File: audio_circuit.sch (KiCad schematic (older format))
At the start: 19 parts

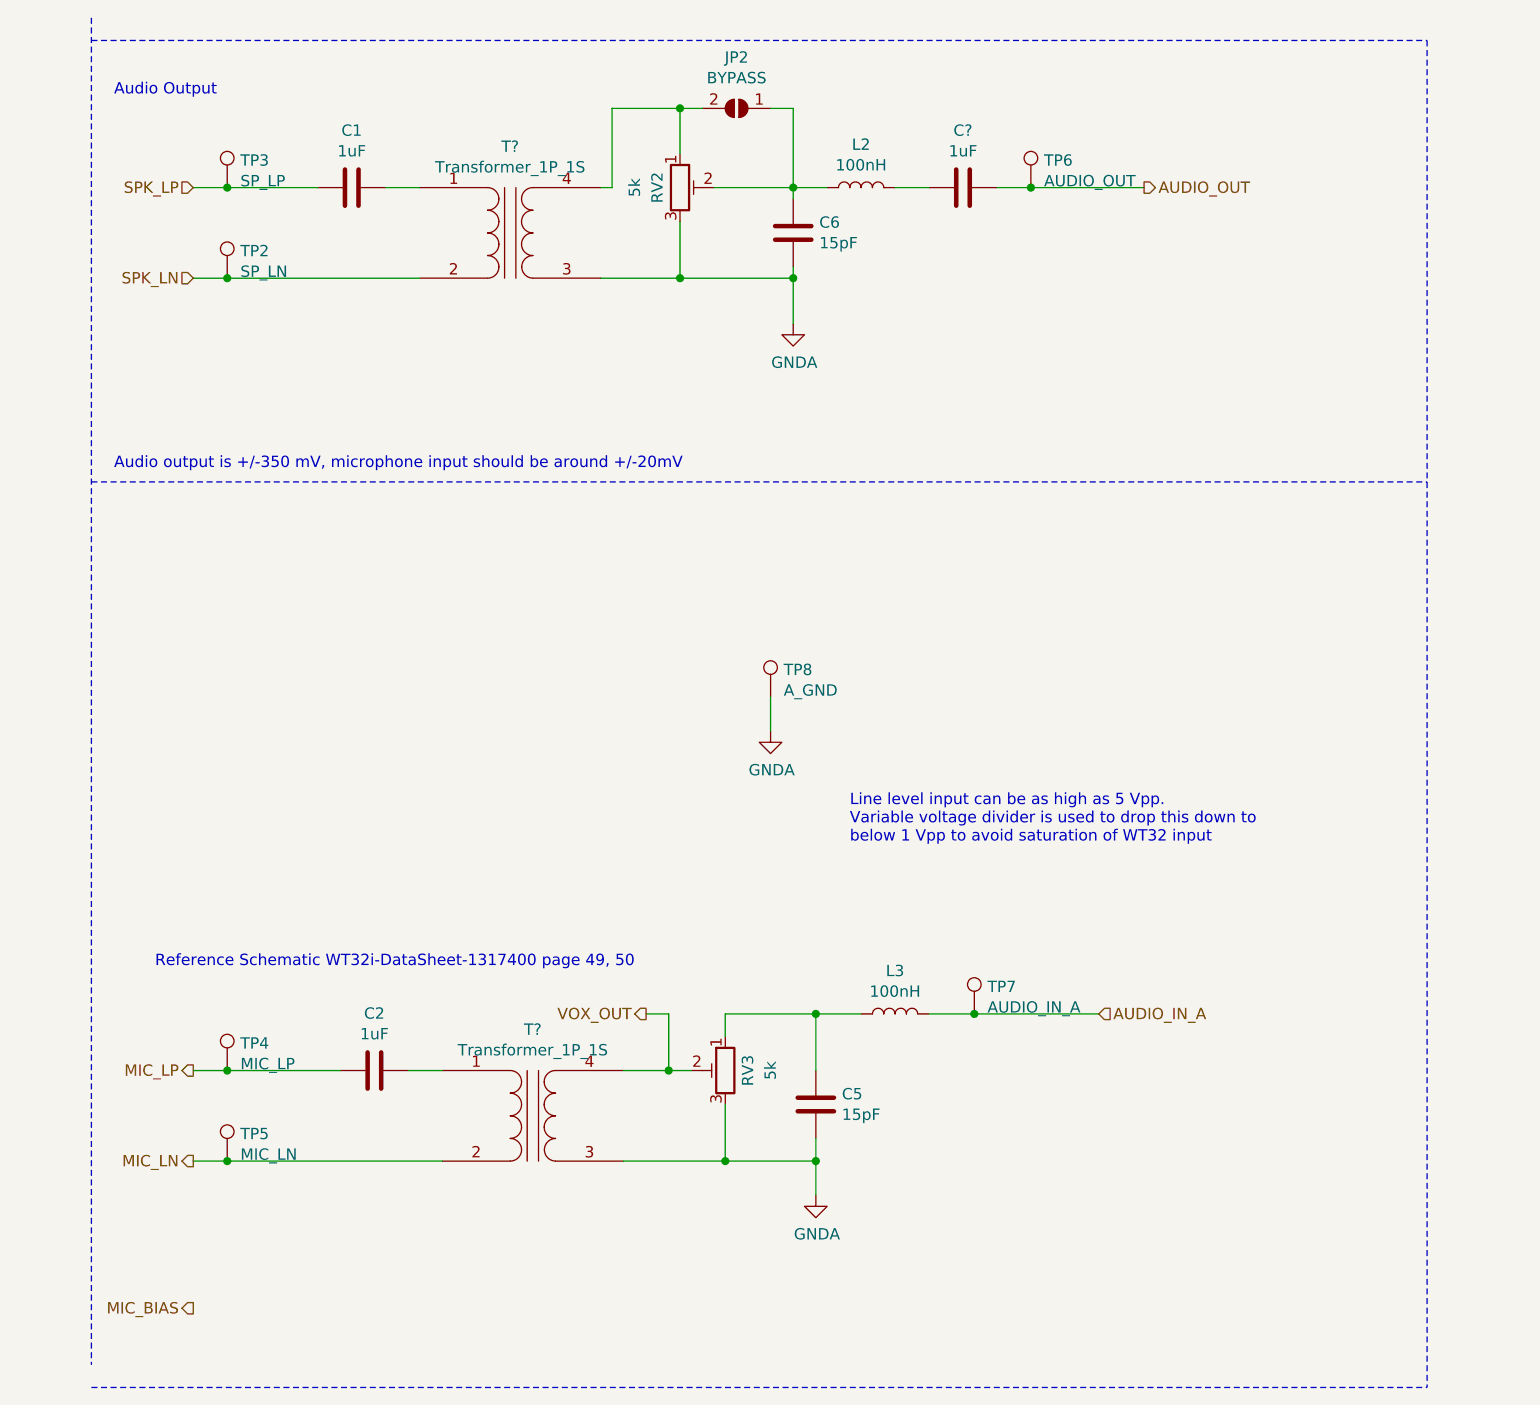
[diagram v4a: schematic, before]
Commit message: Further Audio Rework, separation of AGND and MIC_GND [#21]
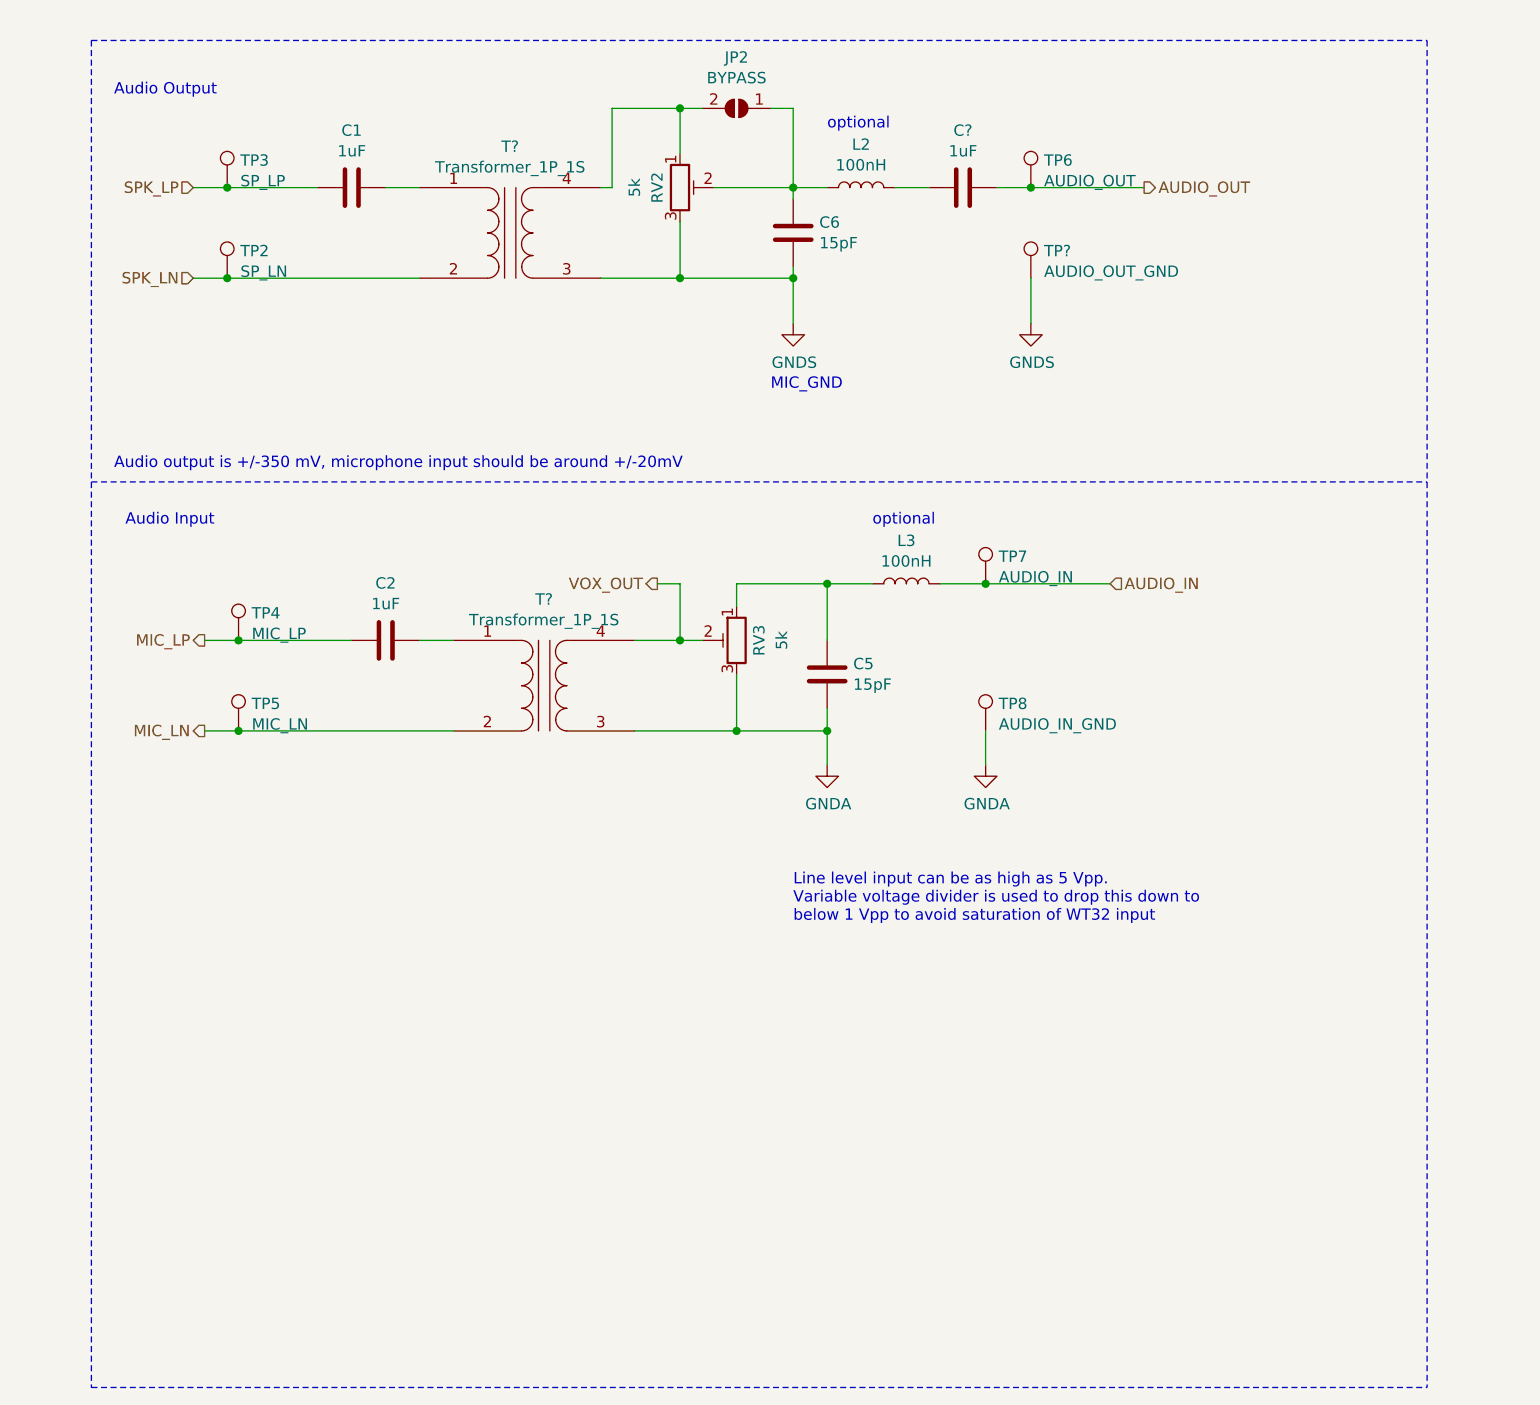
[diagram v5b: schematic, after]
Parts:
- added TP?: AUDIO_OUT_GND, TestPoint:TestPoint_Pad_4.0x4.0mm, symbol Connector:TestPoint
- TP7: value AUDIO_IN_A -> AUDIO_IN
- TP8: value A_GND -> AUDIO_IN_GND
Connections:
- net GNDA: no longer C6.2, RV2.3, T?.3 (SA)
- net AUDIO_IN_A renamed AUDIO_IN
- new net GNDS: C6.2, RV2.3, T?.3 (SA), TP?.1
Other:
- note added: "Audio Input"
- note added: "MIC_GND"
- note added: "optional"
- note removed: "Reference Schematic WT32i-DataSheet-1317400 page 49, 50"
- moved on the sheet: C2, C5, L3, RV3, T?, TP4, TP5, TP7, TP8

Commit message: Continued Schematic for V5.0
* Rearanged RJ45 connector
* Added jumper wire connector
* Renamed GNDs
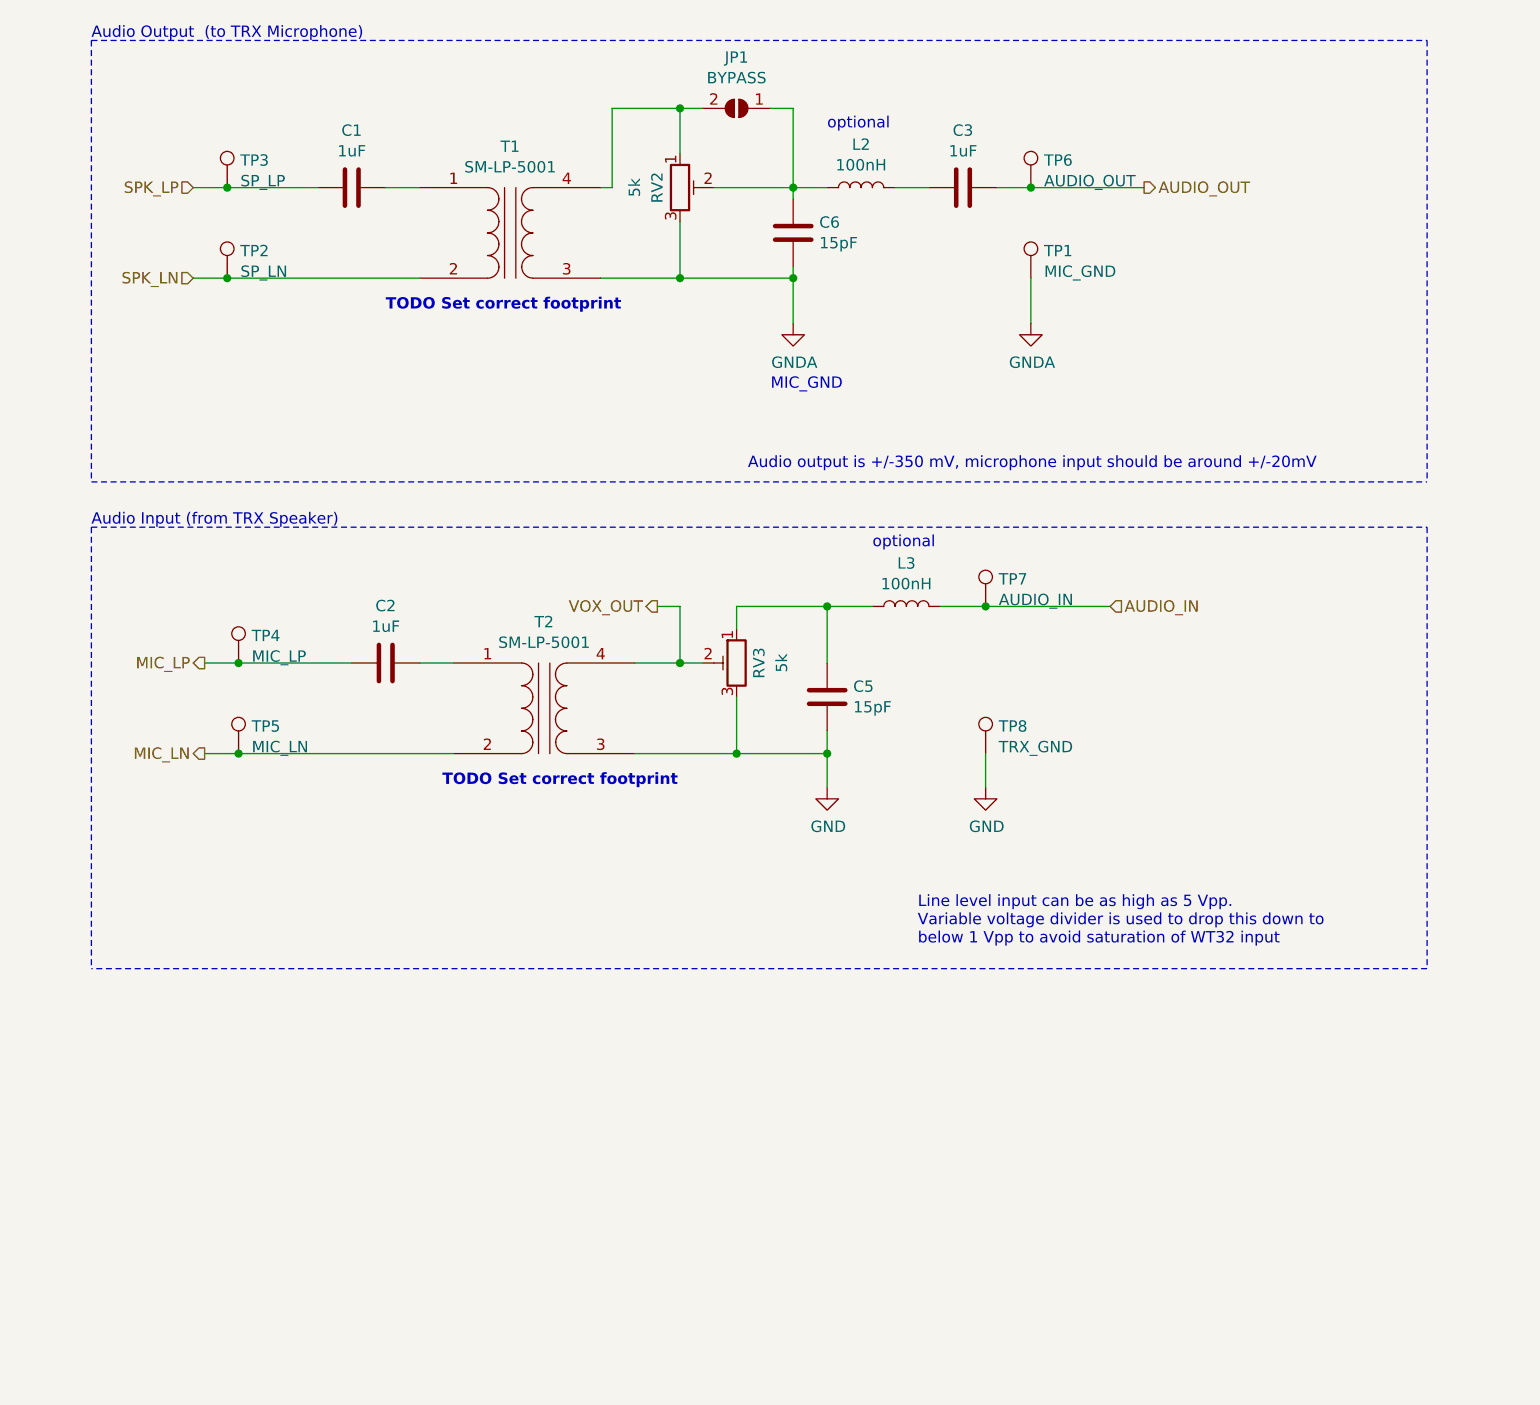
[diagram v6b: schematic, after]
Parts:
- T1, T2: renamed from T?; value Transformer_1P_1S -> SM-LP-5001
- TP1: renamed from TP?; value AUDIO_OUT_GND -> MIC_GND
- TP8: value AUDIO_IN_GND -> TRX_GND
- gave numbers to parts that had none: 1
- renumbered JP2 to JP1
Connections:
- net GNDS is gone; now on net GNDA: C6.2, RV2.3, T1.3 (SA), TP1.1
- net GNDA: no longer C5.2, RV3.3, T2.3 (SA), TP8.1
- new net GND: C5.2, RV3.3, T2.3 (SA), TP8.1
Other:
- note added: "Audio Input (from TRX Speaker)"
- note added: "Audio Output (to TRX Microphone)"
- note added: "TODO Set correct footprint"
- note removed: "Audio Input"
- note removed: "Audio Output"
- moved on the sheet: C2, C5, L3, RV3, T2, TP4, TP5, TP7, TP8

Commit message: Added Footprints [#21]
* Footprint LTV-816S
* Footprint SML-P-5001
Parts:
- C1: footprint Capacitor_SMD:C_0805_2012Metric_Pad1.15x1.40mm_HandSolder -> liteon:LTV-816S
- T1, T2: footprint (none) -> bourns:SM-LP-5001; symbol Device:Transformer_1P_1S -> Transformer:PA1323NL
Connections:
- net GND: now also T2.4; no longer T2.3 (SA)
- net GNDA: now also T1.4; no longer T1.3 (SA)
- net MIC_LN: now also T2.3; no longer T2.2 (AB)
- net SPK_LN: now also T1.3; no longer T1.2 (AB)
- net VOX_OUT: now also T2.6; no longer T2.4 (SB)
- net at JP1.2 (B), RV2.1: now also T1.6; no longer T1.4 (SB)
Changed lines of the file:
@@
 F 0 "C1" V 1698 1900 50  0000 C CNN
 F 1 "1uF" V 1789 1900 50  0000 C CNN
-F 2 "Capacitor_SMD:C_0805_2012Metric_Pad1.15x1.40mm_HandSolder" H 1988 1750 50  0001 C CNN
+F 2 "liteon:LTV-816S" H 1988 1750 50  0001 C CNN
 F 3 "~" H 1950 1900 50  0001 C CNN
 F 4 "80-C0805C105K3RAUTO" H 50  -4100 50  0001 C CNN "Mouser Best.Nr."
@@
 VOX_OUT
 $Comp
-L Device:Transformer_1P_1S T1
+L Transformer:PA1323NL T1
 U 1 1 5E2085AD
 P 2650 2100
 F 0 "T1" H 2650 2481 50  0000 C CNN
 F 1 "SM-LP-5001" H 2650 2390 50  0000 C CNN
-F 2 "" H 2650 2100 50  0001 C CNN
+F 2 "bourns:SM-LP-5001" H 2650 2100 50  0001 C CNN
 F 3 "~" H 2650 2100 50  0001 C CNN
 	1    2650 2100
@@
 	1400 1900 1800 1900
 Connection ~ 1400 1900
-Wire Wire Line
-	2100 1900 2250 1900
-Wire Wire Line
-	2250 2300 1400 2300
 Connection ~ 1400 2300
 $Comp
-L Device:Transformer_1P_1S T2
+L Transformer:PA1323NL T2
 U 1 1 5E232E72
 P 2800 4200
 F 0 "T2" H 2800 4581 50  0000 C CNN
 F 1 "SM-LP-5001" H 2800 4490 50  0000 C CNN
-F 2 "" H 2800 4200 50  0001 C CNN
+F 2 "bourns:SM-LP-5001" H 2800 4200 50  0001 C CNN
 F 3 "~" H 2800 4200 50  0001 C CNN
 	1    2800 4200
@@
 $EndComp
 Wire Wire Line
-	2250 4000 2400 4000
-Wire Wire Line
-	1450 4400 2400 4400
-Wire Wire Line
-	3200 4000 3400 4000
-Wire Wire Line
 	3650 3850 3650 3750
 Wire Wire Line
@@
 Wire Wire Line
 	4050 3750 4050 4000
-Wire Wire Line
-	3200 4400 3650 4400
 Wire Wire Line
 	4050 4300 4050 4400
@@
 	3550 1900 3900 1900
 Wire Wire Line
-	3050 1900 3100 1900
-Wire Wire Line
 	3400 2050 3400 2300
-Wire Wire Line
-	3050 2300 3400 2300
 Wire Wire Line
 	3400 2300 3900 2300
@@
 	-1   0    0    -1
 $EndComp
+Wire Wire Line
+	2100 1900 2450 1900
+Wire Wire Line
+	1400 2300 2450 2300
+Wire Wire Line
+	2850 1900 3100 1900
+Wire Wire Line
+	2850 2300 3400 2300
+Wire Wire Line
+	2250 4000 2600 4000
+Wire Wire Line
+	1450 4400 2600 4400
+Wire Wire Line
+	3000 4400 3650 4400
+Wire Wire Line
+	3000 4000 3400 4000
 $EndSCHEMATC

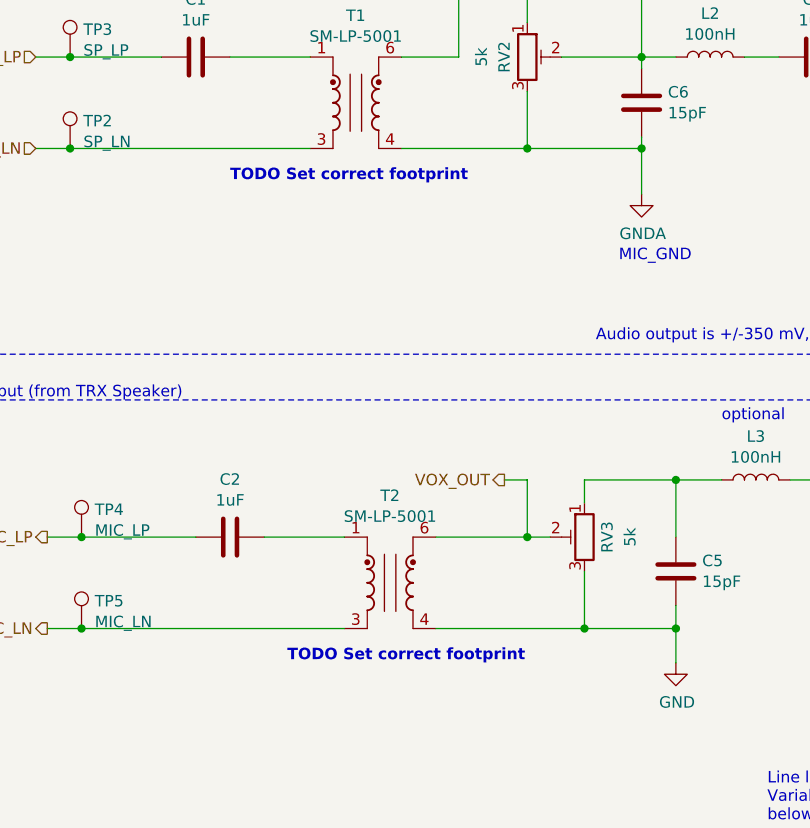
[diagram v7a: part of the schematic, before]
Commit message: Replaced PTT-SEL with solder jumper [#21]
* Replaced PTT-SEL with solder jumper
* Fixed typos in comments
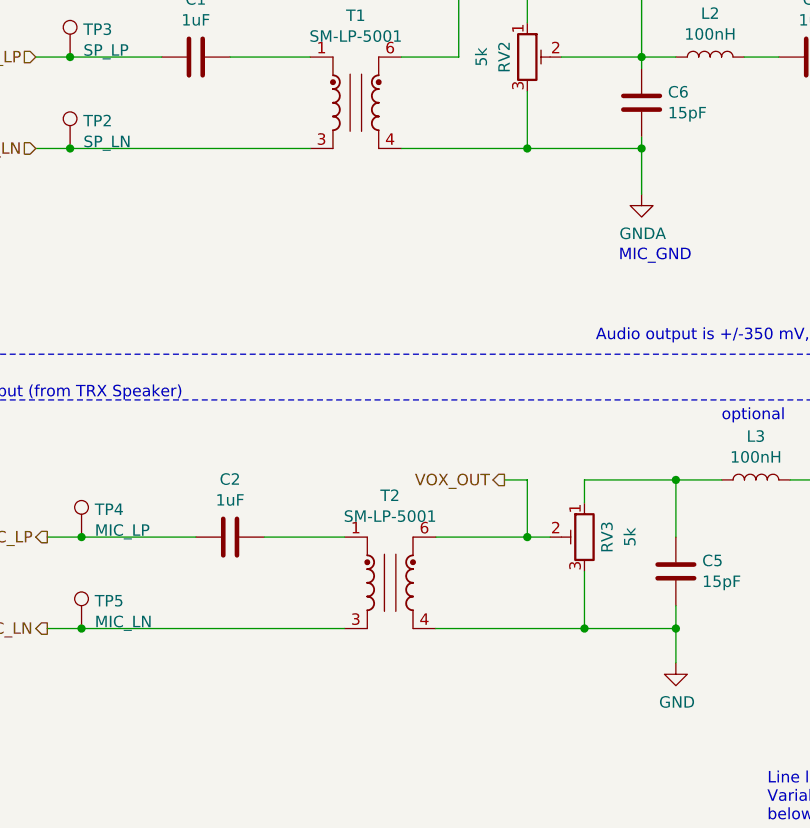
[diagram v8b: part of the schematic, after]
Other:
- note removed: "TODO Set correct footprint"
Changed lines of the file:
@@
 	1    0    0    -1
 $EndComp
-Text Notes 2100 2450 0    50   ~ 10
-TODO Set correct footprint
-Text Notes 2350 4550 0    50   ~ 10
-TODO Set correct footprint
 $Comp
 L Device:R_POT_TRIM RV2
